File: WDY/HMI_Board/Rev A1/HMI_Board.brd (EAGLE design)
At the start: 138 x 36.4 mm, 36 parts, among them SW1 B3FS-1015, SW2 B3FS-1015, SW3 B3FS-1015, SW4 B3FS-1015, SW5 B3FS-1015, SW6 B3FS-1015, U1 90814-0208, U2 90814-0206

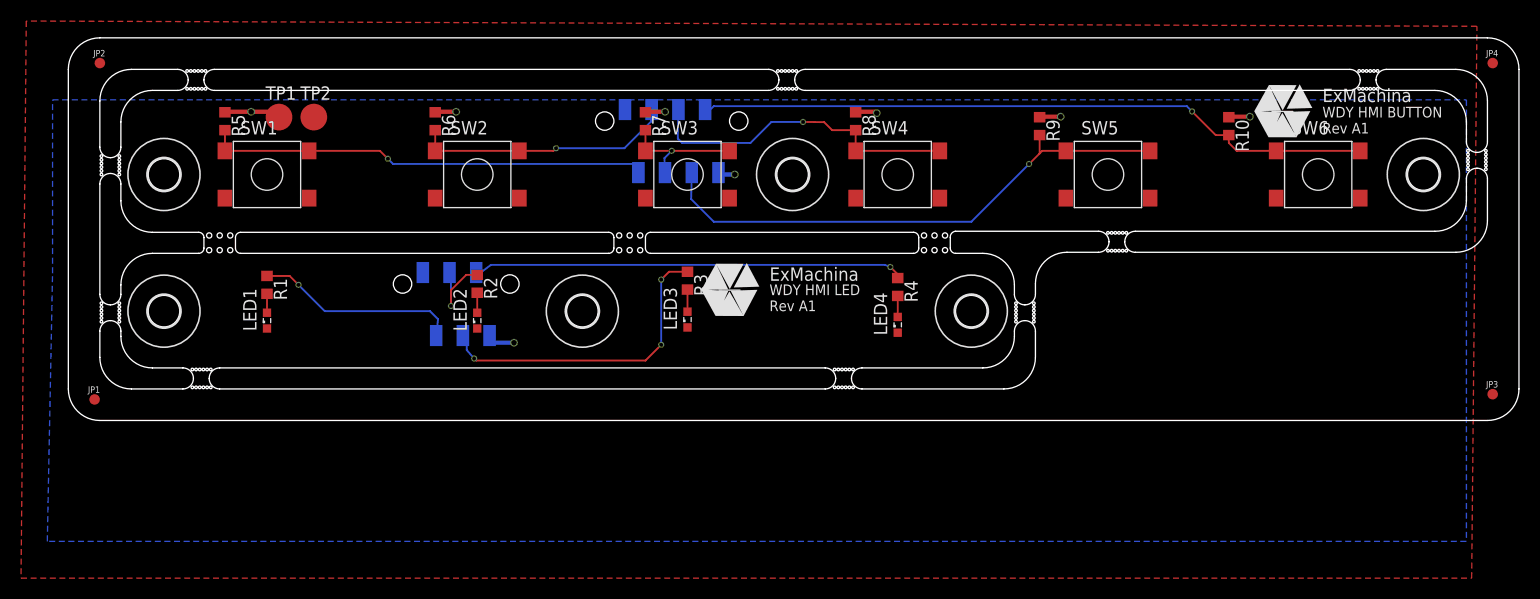
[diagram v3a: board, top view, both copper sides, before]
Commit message: Change LED position and generate gerber
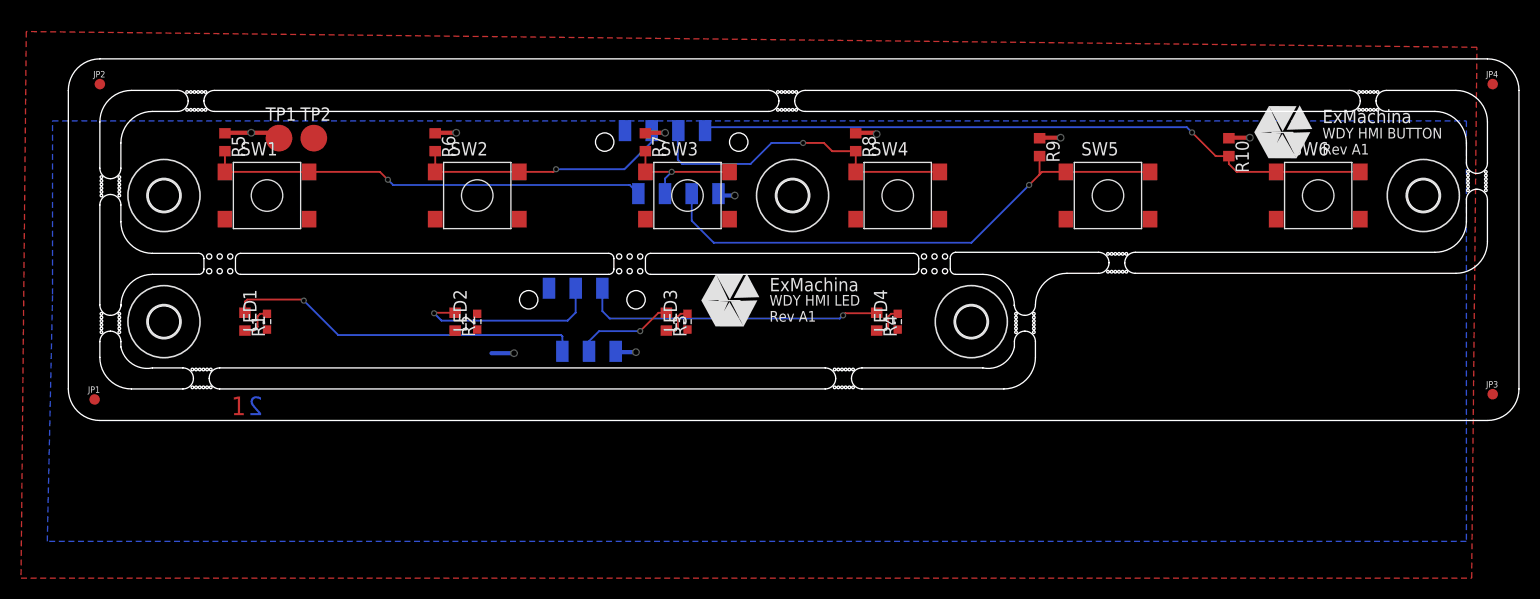
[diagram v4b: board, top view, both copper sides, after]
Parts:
- removed H5: MOUNT-HOLE3.0, holes:3,0
- moved U2 12.1 mm to (48.9, 9.40)
- moved R3 4.38 mm to (56.9, 9.40)
- moved R2 4.17 mm to (36.8, 9.40)
- moved R1 4.08 mm to (16.8, 9.40)
- moved R4 3.86 mm to (76.9, 9.40)
- moved H1 2.00 mm to (128.9, 21.4)
- moved H2 2.00 mm to (68.9, 21.4)
- moved H6 2.00 mm to (9.10, 21.4)
- moved JP2 2.00 mm to (3.00, 32.0)
- moved JP4 2.00 mm to (135.5, 32.0)
- moved R10 2.00 mm to (110.4, 26.0)
- moved R5 2.00 mm to (14.9, 26.5)
- moved R6 2.00 mm to (34.9, 26.5)
- moved R7 2.00 mm to (54.9, 26.5)
- moved R8 2.00 mm to (74.9, 26.5)
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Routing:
- net HMI_LED_3: track 30.0 -> 9.44 mm, vias 3 -> 1
- net HMI_LED_1: track 19.5 -> 34.2 mm
- net HMI_LED_4: track 41.2 -> 29.1 mm
- net HMI_LED_2: track 7.79 -> 18.4 mm
- net N$2: track 1.90 -> 0.00 mm
- net N$1: track 1.80 -> 3.35 mm
- net N$4: track 2.00 -> 3.25 mm
- net N$3: track 2.10 -> 3.31 mm
- net GND: track 4.64 -> 5.73 mm, vias 2 -> 3
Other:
- board size 138 x 36.4 mm -> 138 x 34.4 mm
- board text added: "1"
- board text added: "2"
